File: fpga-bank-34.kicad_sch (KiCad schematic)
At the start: 5 parts, among them U1 XC7K410T-2FFG900I

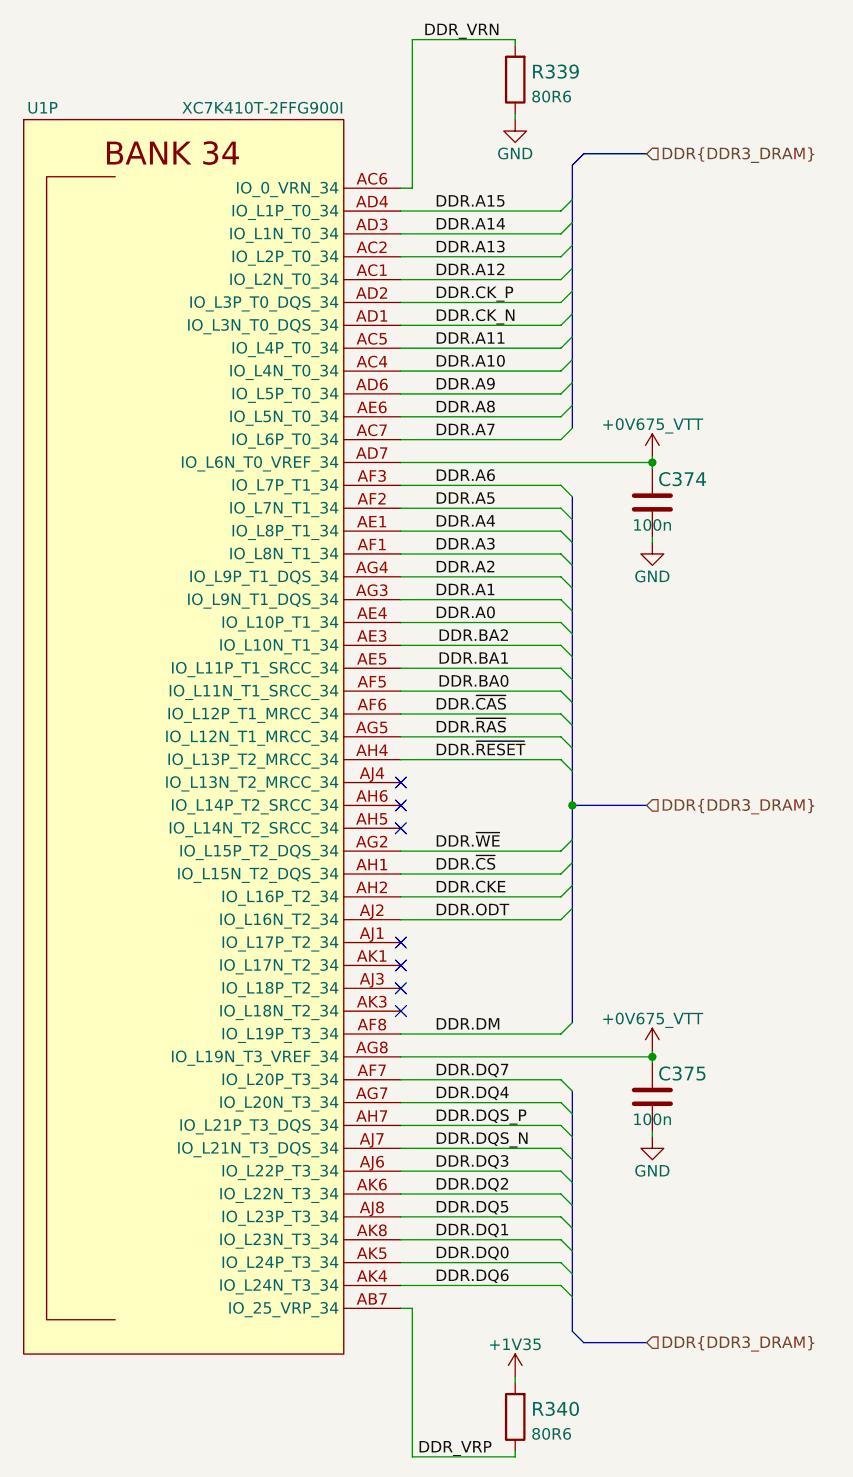
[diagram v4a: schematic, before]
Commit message: Increase 0201 to 0402 components where possible (EIA 0402 footprint)
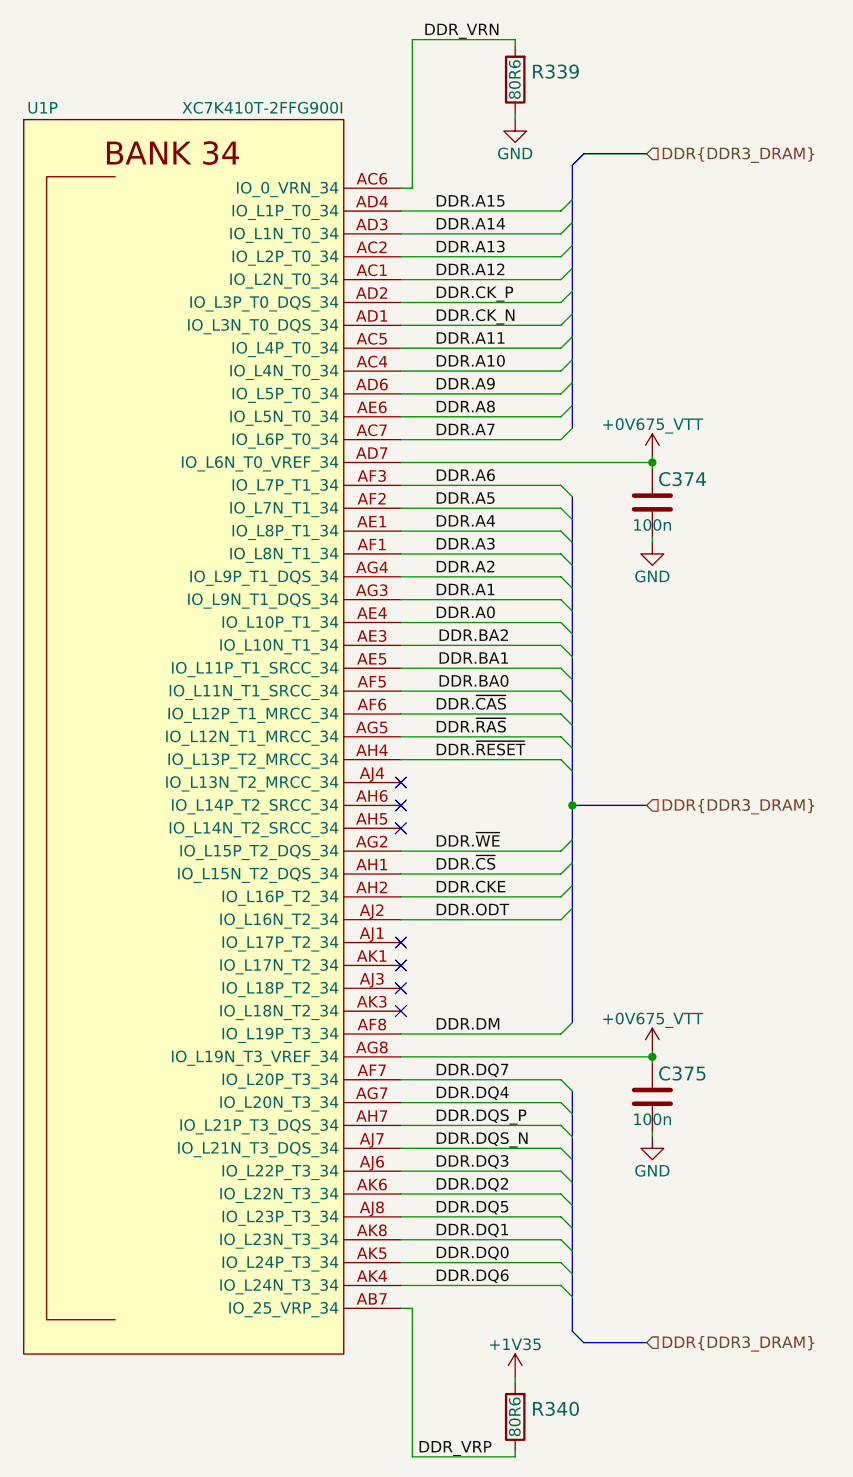
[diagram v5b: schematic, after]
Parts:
- R339, R340: value R_80R6_0402 -> R_80R6_0402_EIA; footprint antmicro-footprints:0402-res -> antmicro-footprints:0402-res_EIA; symbol antmicroResistors0402:R_80R6_0402 -> antmicroResistors0402:R_80R6_0402_EIA
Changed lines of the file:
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@@
     (effects (font (size 1.27 1.27)) (justify left))
   )
-  (symbol (lib_id "antmicroResistors0402:R_80R6_0402") (at 156.21 71.755 90) (unit 1)
-    (in_bom yes) (on_board yes) (fields_autoplaced)
+  (symbol (lib_id "antmicroResistors0402:R_80R6_0402_EIA") (at 156.21 71.755 90) (unit 1)
+    (in_bom yes) (on_board yes)
     (property "Reference" "R339" (id 0) (at 157.988 70.9204 90)
       (effects (font (size 1.524 1.524)) (justify right))
     )
-    (property "Value" "R_80R6_0402" (id 1) (at 160.02 71.755 0)
+    (property "Value" "R_80R6_0402_EIA" (id 1) (at 160.02 71.755 0)
       (effects (font (size 1.524 1.524)) hide)
     )
-    (property "Footprint" "antmicro-footprints:0402-res" (id 2) (at 151.13 66.675 0)
+    (property "Footprint" "antmicro-footprints:0402-res_EIA" (id 2) (at 151.13 66.675 0)
       (effects (font (size 1.524 1.524)) (justify left) hide)
     )
@@
       (effects (font (size 1.524 1.524)) (justify left) hide)
     )
-    (property "Val" "80R6" (id 6) (at 157.988 73.6855 90)
-      (effects (font (size 1.27 1.27)) (justify right))
-    )
+    (property "Val" "80R6" (id 6) (at 156.21 71.755 0))
     (pin "1")
     (pin "2")
   )
-  (symbol (lib_id "antmicroResistors0402:R_80R6_0402") (at 156.21 220.345 90) (unit 1)
-    (in_bom yes) (on_board yes) (fields_autoplaced)
+  (symbol (lib_id "antmicroResistors0402:R_80R6_0402_EIA") (at 156.21 220.345 90) (unit 1)
+    (in_bom yes) (on_board yes)
     (property "Reference" "R340" (id 0) (at 157.988 219.5104 90)
       (effects (font (size 1.524 1.524)) (justify right))
     )
-    (property "Value" "R_80R6_0402" (id 1) (at 160.02 220.345 0)
+    (property "Value" "R_80R6_0402_EIA" (id 1) (at 160.02 220.345 0)
       (effects (font (size 1.524 1.524)) hide)
     )
-    (property "Footprint" "antmicro-footprints:0402-res" (id 2) (at 151.13 215.265 0)
+    (property "Footprint" "antmicro-footprints:0402-res_EIA" (id 2) (at 151.13 215.265 0)
       (effects (font (size 1.524 1.524)) (justify left) hide)
     )
@@
       (effects (font (size 1.524 1.524)) (justify left) hide)
     )
-    (property "Val" "80R6" (id 6) (at 157.988 222.2755 90)
-      (effects (font (size 1.27 1.27)) (justify right))
-    )
+    (property "Val" "80R6" (id 6) (at 156.21 220.345 0))
     (pin "1")
     (pin "2")

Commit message: Loclib
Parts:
- C374, C375: footprint antmicro-footprints:0402-cap_EIA -> K410T-devboard-footprints:0402-cap_EIA; symbol antmicroCapacitors0402:C_100n_0402_EIA -> K410T-devboard:C_100n_0402_EIA
- R339, R340: footprint antmicro-footprints:0402-res_EIA -> K410T-devboard-footprints:0402-res_EIA; symbol antmicroResistors0402:R_80R6_0402_EIA -> K410T-devboard:R_80R6_0402_EIA
- U1: footprint antmicro-footprints:xc7k410t-2ffg900I -> K410T-devboard-footprints:xc7k410t-2ffg900I; symbol antmicroMicrocontrollers:XC7K410T-2FFG900I -> K410T-devboard:XC7K410T-2FFG900I
